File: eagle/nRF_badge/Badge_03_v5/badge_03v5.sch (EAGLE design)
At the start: 45 parts, among them J1 PROG_CONN_6, U1 AT25M02, U2 LP2985LV, U3 MCP6231, U4 PCF85263, Y1 32768Hz, Y2 32768Hz

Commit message: Added BU2032SM variant with cream. Changed BAT4 (top) to use cream
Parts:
- BAT1: device Badge:BATTERY20MM_ISO_NO_CENTER_CREAM -> Badge:BATTERY20MM_ISO_NOCREAM
- BAT4: device Badge:BATTERYHOLDER -> Badge:BATTERYBU2032SM_CREAM
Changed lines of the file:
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@@
 <part name="R3" library="rcl" deviceset="R-US_" device="R0603" value="1k"/>
 <part name="R2" library="rcl" deviceset="R-US_" device="R0603" value="1k"/>
-<part name="BAT1" library="Badge" deviceset="BATTERY" device="20MM_ISO_NO_CENTER_CREAM" value="CR2032"/>
+<part name="BAT1" library="Badge" deviceset="BATTERY" device="20MM_ISO_NOCREAM" value="CR2032"/>
 <part name="C1" library="rcl" deviceset="C-EU" device="C1206" value="100u"/>
 <part name="C6" library="rcl" deviceset="C-EU" device="C0603" value="1u"/>
@@
 <part name="M_RAW" library="Badge" deviceset="TESTPOINT" device="" value=""/>
 <part name="C2" library="rcl" deviceset="C-EU" device="C0603" value="0u1"/>
-<part name="BAT4" library="Badge" deviceset="BATTERY" device="HOLDER" value="CR2032"/>
+<part name="BAT4" library="Badge" deviceset="BATTERY" device="BU2032SM_CREAM" value="CR2032"/>
 <part name="MIC_F" library="Badge" deviceset="TESTPOINT" device="" value=""/>
 <part name="M_VCC" library="Badge" deviceset="TESTPOINT" device="" value=""/>

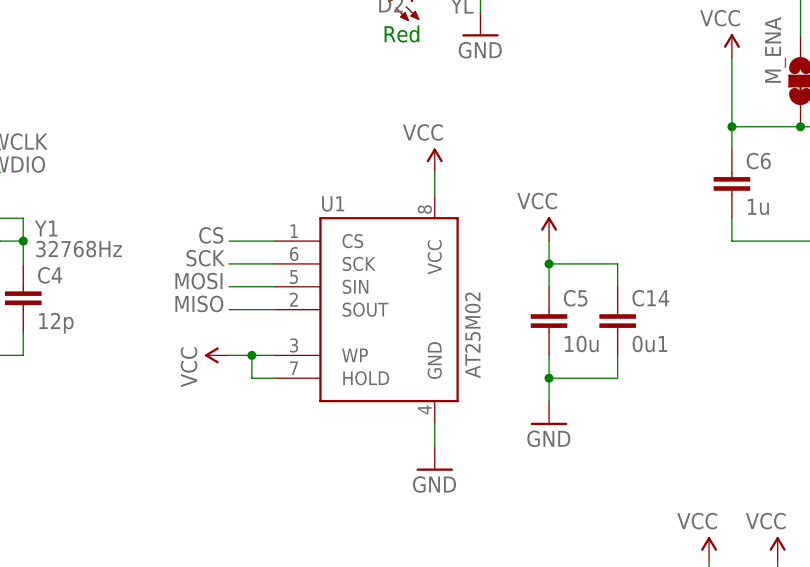
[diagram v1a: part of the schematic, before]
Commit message: Replaced AT25M02 with M95M02
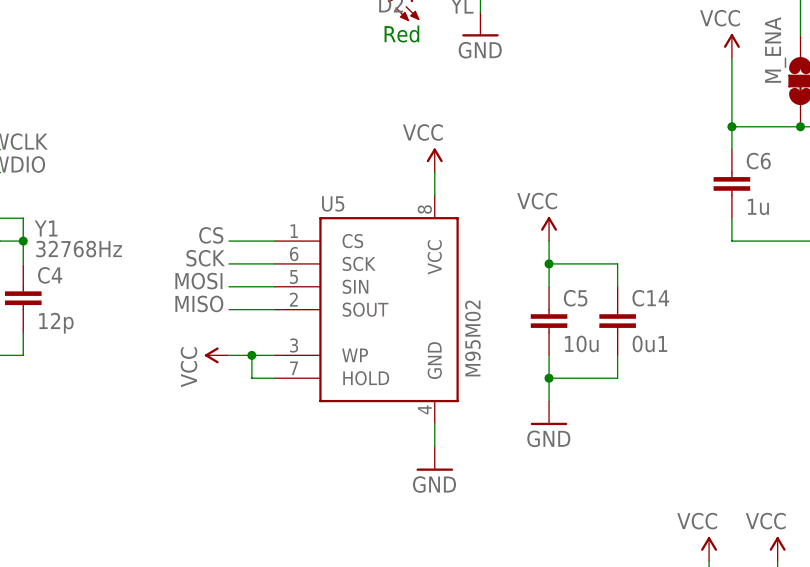
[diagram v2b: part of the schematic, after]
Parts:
- removed U1: AT25M02, Badge:AT25M02_SOIC
- added U5: M95M02, Badge:M95M02_SOIC
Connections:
- net CS: now also U5.CS; no longer U1.CS
- net GND: now also U5.GND; no longer U1.GND
- net MISO: now also U5.SOUT; no longer U1.SOUT
- net MOSI: now also U5.SIN; no longer U1.SIN
- net SCK: now also U5.SCK; no longer U1.SCK
- net VCC: now also U5.HOLD, U5.VCC, U5.WP; no longer U1.HOLD, U1.VCC, U1.WP
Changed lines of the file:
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@@
 <grid distance="0.1" unitdist="inch" unit="inch" style="lines" multiple="1" display="no" altdistance="0.01" altunitdist="inch" altunit="inch"/>
 <layers>
-<layer number="1" name="Top" color="4" fill="1" visible="yes" active="no"/>
-<layer number="16" name="Bottom" color="1" fill="1" visible="yes" active="no"/>
-<layer number="17" name="Pads" color="2" fill="1" visible="yes" active="no"/>
-<layer number="18" name="Vias" color="2" fill="1" visible="yes" active="no"/>
-<layer number="19" name="Unrouted" color="14" fill="1" visible="yes" active="no"/>
-<layer number="20" name="Dimension" color="15" fill="1" visible="yes" active="no"/>
-<layer number="21" name="tPlace" color="16" fill="1" visible="yes" active="no"/>
-<layer number="22" name="bPlace" color="7" fill="1" visible="yes" active="no"/>
-<layer number="23" name="tOrigins" color="15" fill="1" visible="yes" active="no"/>
-<layer number="24" name="bOrigins" color="15" fill="1" visible="yes" active="no"/>
-<layer number="25" name="tNames" color="7" fill="1" visible="yes" active="no"/>
-<layer number="26" name="bNames" color="7" fill="1" visible="yes" active="no"/>
-<layer number="27" name="tValues" color="7" fill="1" visible="yes" active="no"/>
-<layer number="28" name="bValues" color="7" fill="1" visible="yes" active="no"/>
+<layer number="1" name="Top" color="4" fill="1" visible="no" active="no"/>
+<layer number="16" name="Bottom" color="1" fill="1" visible="no" active="no"/>
+<layer number="17" name="Pads" color="2" fill="1" visible="no" active="no"/>
+<layer number="18" name="Vias" color="2" fill="1" visible="no" active="no"/>
+<layer number="19" name="Unrouted" color="14" fill="1" visible="no" active="no"/>
+<layer number="20" name="Dimension" color="15" fill="1" visible="no" active="no"/>
+<layer number="21" name="tPlace" color="16" fill="1" visible="no" active="no"/>
+<layer number="22" name="bPlace" color="7" fill="1" visible="no" active="no"/>
+<layer number="23" name="tOrigins" color="15" fill="1" visible="no" active="no"/>
+<layer number="24" name="bOrigins" color="15" fill="1" visible="no" active="no"/>
+<layer number="25" name="tNames" color="7" fill="1" visible="no" active="no"/>
+<layer number="26" name="bNames" color="7" fill="1" visible="no" active="no"/>
+<layer number="27" name="tValues" color="7" fill="1" visible="no" active="no"/>
+<layer number="28" name="bValues" color="7" fill="1" visible="no" active="no"/>
 <layer number="29" name="tStop" color="7" fill="3" visible="no" active="no"/>
 <layer number="30" name="bStop" color="7" fill="6" visible="no" active="no"/>
@@
 <layer number="35" name="tGlue" color="7" fill="4" visible="no" active="no"/>
 <layer number="36" name="bGlue" color="7" fill="5" visible="no" active="no"/>
-<layer number="37" name="tTest" color="7" fill="1" visible="yes" active="no"/>
-<layer number="38" name="bTest" color="7" fill="1" visible="yes" active="no"/>
+<layer number="37" name="tTest" color="7" fill="1" visible="no" active="no"/>
+<layer number="38" name="bTest" color="7" fill="1" visible="no" active="no"/>
 <layer number="39" name="tKeepout" color="4" fill="11" visible="no" active="no"/>
 <layer number="40" name="bKeepout" color="1" fill="11" visible="no" active="no"/>
@@
 <layer number="44" name="Drills" color="7" fill="1" visible="no" active="no"/>
 <layer number="45" name="Holes" color="7" fill="1" visible="no" active="no"/>
-<layer number="46" name="Milling" color="3" fill="1" visible="yes" active="no"/>
-<layer number="47" name="Measures" color="7" fill="1" visible="yes" active="no"/>
-<layer number="48" name="Document" color="7" fill="1" visible="yes" active="no"/>
-<layer number="49" name="Reference" color="7" fill="1" visible="yes" active="no"/>
-<layer number="50" name="dxf" color="7" fill="1" visible="yes" active="no"/>
-<layer number="51" name="tDocu" color="6" fill="1" visible="yes" active="no"/>
-<layer number="52" name="bDocu" color="6" fill="1" visible="yes" active="no"/>
-<layer number="53" name="tGND_GNDA" color="7" fill="9" visible="yes" active="no"/>
-<layer number="54" name="bGND_GNDA" color="1" fill="9" visible="yes" active="no"/>
-<layer number="56" name="wert" color="7" fill="1" visible="yes" active="no"/>
-<layer number="57" name="tCAD" color="7" fill="1" visible="yes" active="no"/>
-<layer number="59" name="tCarbon" color="7" fill="1" visible="yes" active="no"/>
-<layer number="60" name="bCarbon" color="7" fill="1" visible="yes" active="no"/>
+<layer number="46" name="Milling" color="3" fill="1" visible="no" active="no"/>
+<layer number="47" name="Measures" color="7" fill="1" visible="no" active="no"/>
+<layer number="48" name="Document" color="7" fill="1" visible="no" active="no"/>
+<layer number="49" name="Reference" color="7" fill="1" visible="no" active="no"/>
+<layer number="50" name="dxf" color="7" fill="1" visible="no" active="no"/>
+<layer number="51" name="tDocu" color="6" fill="1" visible="no" active="no"/>
+<layer number="52" name="bDocu" color="6" fill="1" visible="no" active="no"/>
+<layer number="53" name="tGND_GNDA" color="7" fill="9" visible="no" active="no"/>
+<layer number="54" name="bGND_GNDA" color="1" fill="9" visible="no" active="no"/>
+<layer number="56" name="wert" color="7" fill="1" visible="no" active="no"/>
+<layer number="57" name="tCAD" color="7" fill="1" visible="no" active="no"/>
+<layer number="59" name="tCarbon" color="7" fill="1" visible="no" active="no"/>
+<layer number="60" name="bCarbon" color="7" fill="1" visible="no" active="no"/>
 <layer number="90" name="Modules" color="5" fill="1" visible="yes" active="yes"/>
 <layer number="91" name="Nets" color="2" fill="1" visible="yes" active="yes"/>
@@
 <part name="U4" library="Badge" deviceset="PCF85263" device=""/>
 <part name="SUPPLY2" library="Badge" deviceset="VCC" device=""/>
-<part name="U1" library="Badge" deviceset="AT25M02" device="_SOIC" value="AT25M02"/>
+<part name="U5" library="Badge" deviceset="M95M02" device="_SOIC" value="M95M02"/>
 </parts>
 <sheets>
@@
 <instance part="U4" gate="G$1" x="175.26" y="30.48"/>
 <instance part="SUPPLY2" gate="G$1" x="76.2" y="114.3" rot="MR0"/>
-<instance part="U1" gate="G$1" x="121.92" y="78.74"/>
+<instance part="U5" gate="G$1" x="121.92" y="78.74"/>
 </instances>
 <busses>
@@
 <pinref part="GND8" gate="1" pin="GND"/>
 <wire x1="129.54" y1="63.5" x2="129.54" y2="66.04" width="0.1524" layer="91"/>
-<pinref part="U1" gate="G$1" pin="GND"/>
+<pinref part="U5" gate="G$1" pin="GND"/>
 </segment>
 <segment>
@@
 <pinref part="SUPPLY10" gate="G$1" pin="VCC"/>
 <wire x1="129.54" y1="93.98" x2="129.54" y2="91.44" width="0.1524" layer="91"/>
-<pinref part="U1" gate="G$1" pin="VCC"/>
+<pinref part="U5" gate="G$1" pin="VCC"/>
 </segment>
 <segment>
@@
 <junction x="109.22" y="73.66"/>
 <wire x1="109.22" y1="71.12" x2="111.76" y2="71.12" width="0.1524" layer="91"/>
-<pinref part="U1" gate="G$1" pin="WP"/>
-<pinref part="U1" gate="G$1" pin="HOLD"/>
+<pinref part="U5" gate="G$1" pin="WP"/>
+<pinref part="U5" gate="G$1" pin="HOLD"/>
 </segment>
 <segment>
@@
 <wire x1="111.76" y1="83.82" x2="106.68" y2="83.82" width="0.1524" layer="91"/>
 <label x="106.172" y="85.344" size="1.778" layer="95" rot="R180"/>
-<pinref part="U1" gate="G$1" pin="SCK"/>
+<pinref part="U5" gate="G$1" pin="SCK"/>
 </segment>
 <segment>
@@
 <wire x1="111.76" y1="81.28" x2="106.68" y2="81.28" width="0.1524" layer="91"/>
 <label x="106.172" y="82.804" size="1.778" layer="95" rot="R180"/>
-<pinref part="U1" gate="G$1" pin="SIN"/>
+<pinref part="U5" gate="G$1" pin="SIN"/>
 </segment>
 <segment>
@@
 <wire x1="111.76" y1="78.74" x2="106.68" y2="78.74" width="0.1524" layer="91"/>
 <label x="106.172" y="80.264" size="1.778" layer="95" rot="R180"/>
-<pinref part="U1" gate="G$1" pin="SOUT"/>
+<pinref part="U5" gate="G$1" pin="SOUT"/>
 </segment>
 <segment>
@@
 <wire x1="111.76" y1="86.36" x2="106.68" y2="86.36" width="0.1524" layer="91"/>
 <label x="106.172" y="87.884" size="1.778" layer="95" rot="R180"/>
-<pinref part="U1" gate="G$1" pin="CS"/>
-</segment>
-</net>
+<pinref part="U5" gate="G$1" pin="CS"/>
+</segment>
+</net>

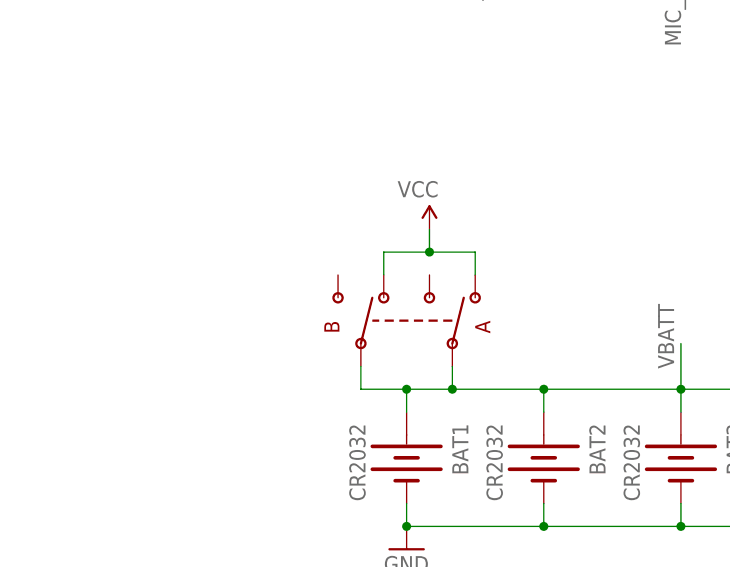
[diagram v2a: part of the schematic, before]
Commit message: Replaced switch with AYZ0202
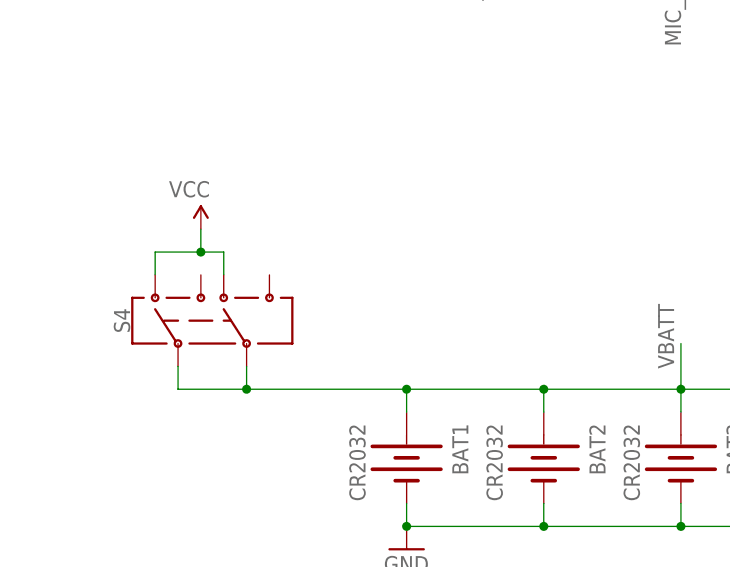
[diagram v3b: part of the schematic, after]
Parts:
- removed S1: DPDT, Badge:JS202011SCQN
- added S4: (no value), Badge:SWITCH-DPDT-SMD-AYZ0202
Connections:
- net VBATT: now also S4.2, S4.5; no longer S1.AC, S1.BC
- net VCC: now also S4.1, S4.4; no longer S1.A1, S1.B1

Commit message: Minor changes. Generated centroids and bom
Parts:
- S4: value (none) -> DPDT
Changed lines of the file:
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@@
 <part name="SUPPLY2" library="Badge" deviceset="VCC" device=""/>
 <part name="U5" library="Badge" deviceset="M95M02" device="_SOIC" value="M95M02"/>
-<part name="S4" library="Badge" deviceset="SWITCH-DPDT" device="-SMD-AYZ0202"/>
+<part name="S4" library="Badge" deviceset="SWITCH-DPDT" device="-SMD-AYZ0202" value="DPDT"/>
 <part name="SUPPLY15" library="Badge" deviceset="VCC" device=""/>
 </parts>
